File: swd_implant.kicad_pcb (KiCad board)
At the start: 2 copper layers, 13.9 x 38.5 mm, 28 parts, among them J1 U262-161N-4BVC11, J2 G&W pressure contact, J3 50 mil Pin Header, J4 SOICbite, J5 100 mil Pin Header, J6 100 mil Pin header, U1 ATSAMD21E18A, U2 AP2127K-3.3

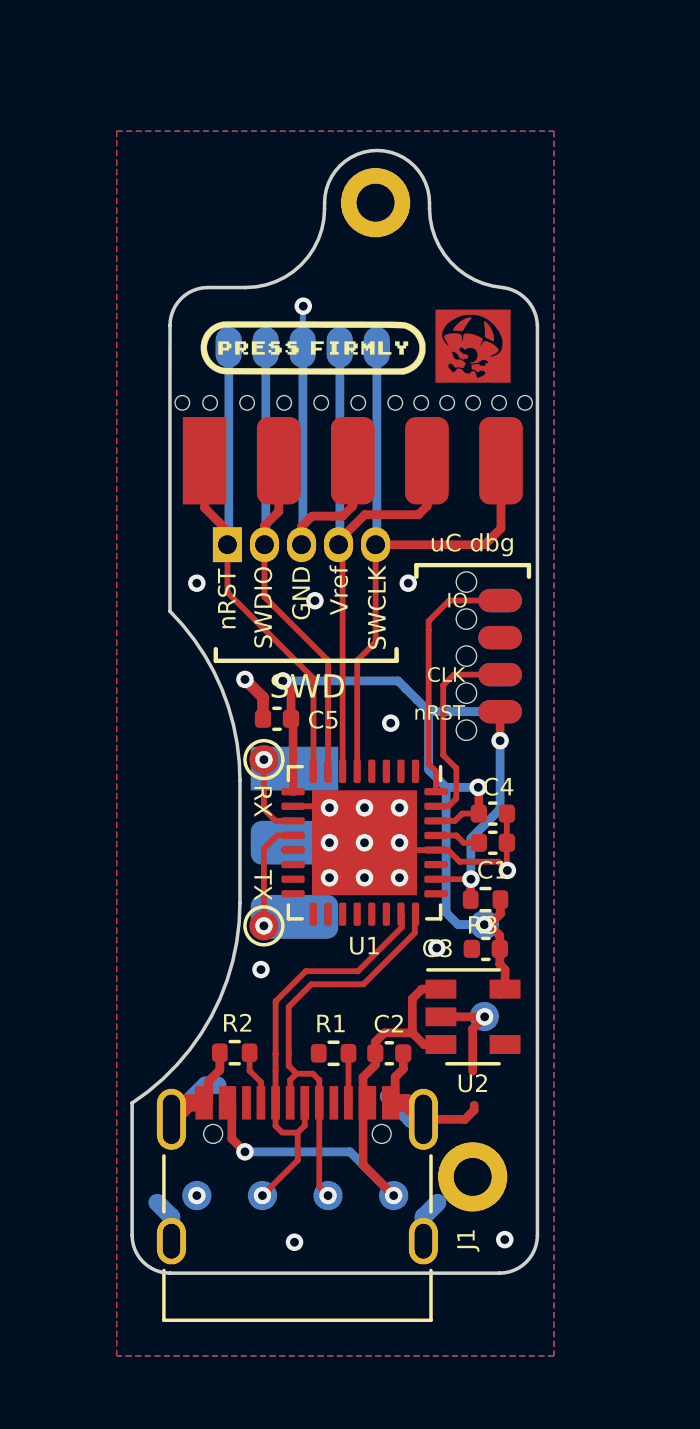
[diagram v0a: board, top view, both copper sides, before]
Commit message: New board outline & swd pinout fixes
Changed the board outline to work with castellated edges, making it possible to
solder down instead of just relying on pressure contact.

Also fixed the inverted SWD pinout from upstream.
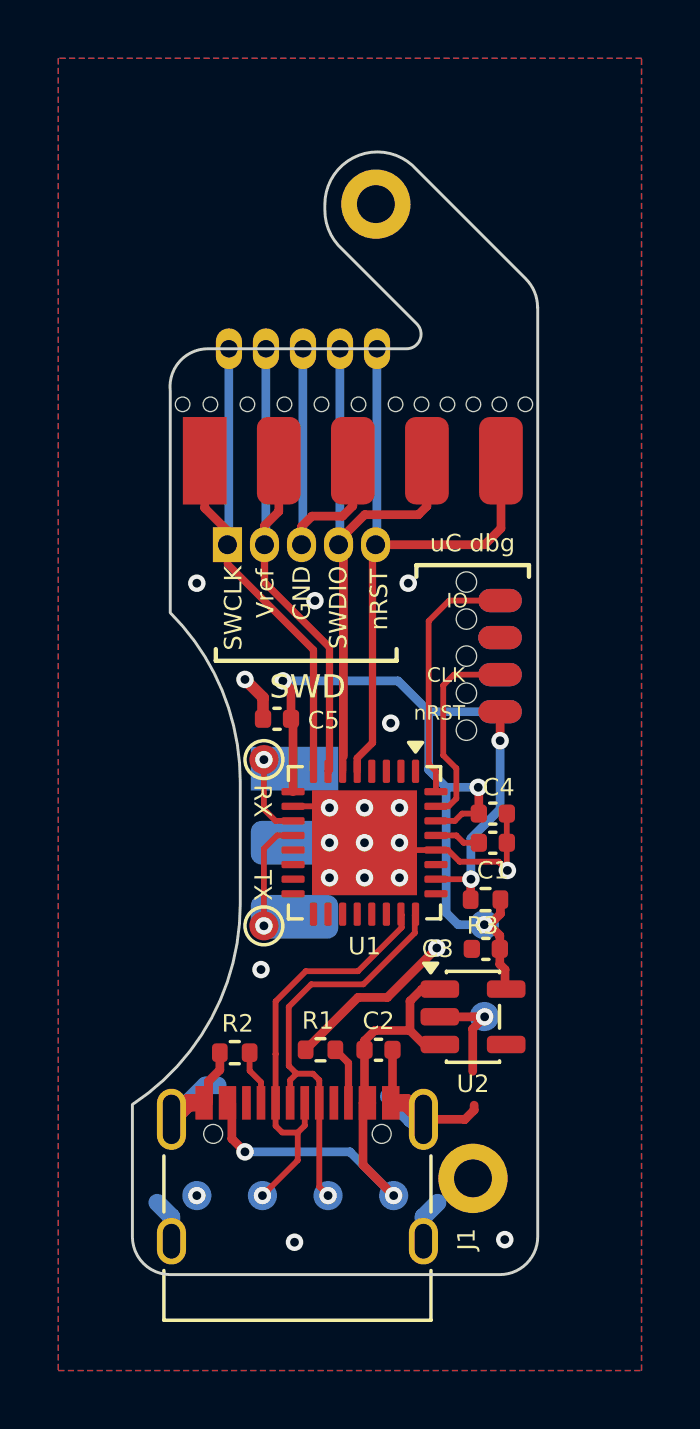
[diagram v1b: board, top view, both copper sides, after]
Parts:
- removed the Ref** at (64.2, 99.9)
- removed the Ref** at (58.7, 99.9)
- removed the Ref** at (59.2, 123.0)
- J2: value G&W pressure contact -> G&W pressure contact
- moved R1 0.47 mm to (59.0, 124.0)
- moved Ref** 0.43 mm to (60.2, 104.7)
- moved C2 0.39 mm to (61.0, 124.0)
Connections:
- net /~RESET~ renamed /~{RESET}
- J1 pad A8: no_connect_18 -> unconnected-(J1-SBU1-PadA8)
- J1 pad B8: no_connect_19 -> unconnected-(J1-SBU2-PadB8)
- J2 pad 1: /GnW_NRST -> /GnW_SWCLK
- J2 pad 2: /GnW_SWDIO -> /GnW_Vref
- J2 pad 4: /GnW_Vref -> /GnW_SWDIO
- J2 pad 5: /GnW_SWCLK -> /GnW_NRST
- J2 pad 6: GND -> (no net)
- J3 pad 1: /GnW_NRST -> /GnW_SWCLK
- J3 pad 2: /GnW_SWDIO -> /GnW_Vref
- J3 pad 4: /GnW_Vref -> /GnW_SWDIO
- J3 pad 5: /GnW_SWCLK -> /GnW_NRST
- J4 pad 2: no_connect_20 -> unconnected-(J4-Pin_2-Pad2)
- J4 pad 3: no_connect_21 -> unconnected-(J4-Pin_3-Pad3)
- J4 pad 6: no_connect_22 -> unconnected-(J4-Pin_6-Pad6)
- J5 pad 1: /GnW_NRST -> /GnW_SWCLK
- J5 pad 2: /GnW_SWDIO -> /GnW_Vref
- J5 pad 4: /GnW_Vref -> /GnW_SWDIO
- J5 pad 5: /GnW_SWCLK -> /GnW_NRST
- U1 pad 1: no_connect_23 -> unconnected-(U1-PA00-Pad1)
- U1 pad 13: no_connect_24 -> unconnected-(U1-PA10-Pad13)
- U1 pad 14: no_connect_25 -> unconnected-(U1-PA11-Pad14)
- U1 pad 15: no_connect_26 -> unconnected-(U1-PA14-Pad15)
- U1 pad 16: no_connect_27 -> unconnected-(U1-PA15-Pad16)
- U1 pad 17: no_connect_28 -> unconnected-(U1-PA16-Pad17)
- U1 pad 18: no_connect_29 -> unconnected-(U1-PA17-Pad18)
- U1 pad 19: no_connect_30 -> unconnected-(U1-PA18-Pad19)
- U1 pad 2: no_connect_31 -> unconnected-(U1-PA01-Pad2)
- U1 pad 20: no_connect_32 -> unconnected-(U1-PA19-Pad20)
- U1 pad 21: no_connect_33 -> unconnected-(U1-PA22-Pad21)
- U1 pad 22: no_connect_34 -> unconnected-(U1-PA23-Pad22)
- U1 pad 25: no_connect_35 -> unconnected-(U1-PA27-Pad25)
- U1 pad 27: no_connect_36 -> unconnected-(U1-PA28-Pad27)
- U1 pad 3: no_connect_37 -> unconnected-(U1-PA02-Pad3)
- U1 pad 4: no_connect_38 -> unconnected-(U1-PA03-Pad4)
- U1 pad 5: /GnW_SWCLK -> /GnW_NRST
- U1 pad 6: /GnW_Vref -> /GnW_SWDIO
- U1 pad 7: /GnW_SWDIO -> /GnW_Vref
- U1 pad 8: /GnW_NRST -> /GnW_SWCLK
- U2 pad 4: (no net) -> unconnected-(U2-NC-Pad4)
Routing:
- net GND: track 48.5 -> 51.6 mm, vias 22 -> 21
- net /GnW_NRST: track 19.0 -> 21.8 mm
- net /GnW_SWCLK: track 21.8 -> 19.0 mm
- net /GnW_SWDIO: track 18.5 -> 20.2 mm
- net /GnW_Vref: track 20.1 -> 18.6 mm
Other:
- outline, holes or cut-outs redrawn
- board text added: "G&W ${VERSION}"

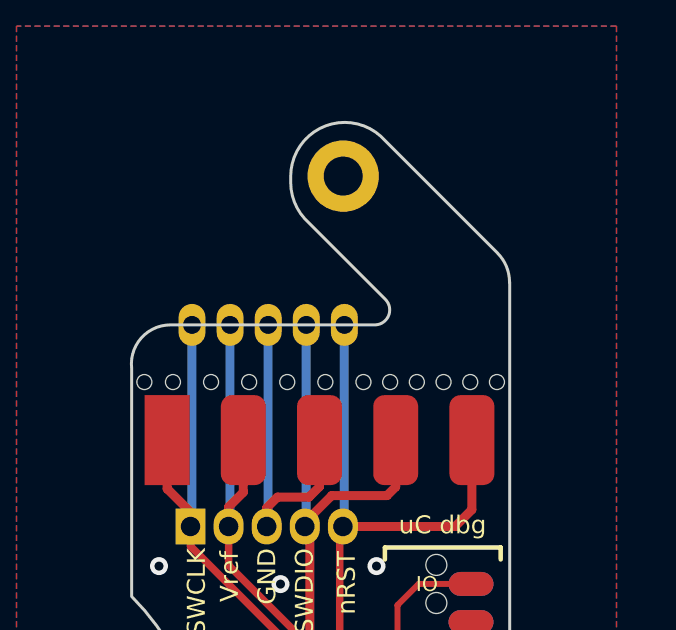
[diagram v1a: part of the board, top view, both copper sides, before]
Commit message: Add M marker to front of board
This M is to indicate that it is the "Mario" variant of the implant
board.
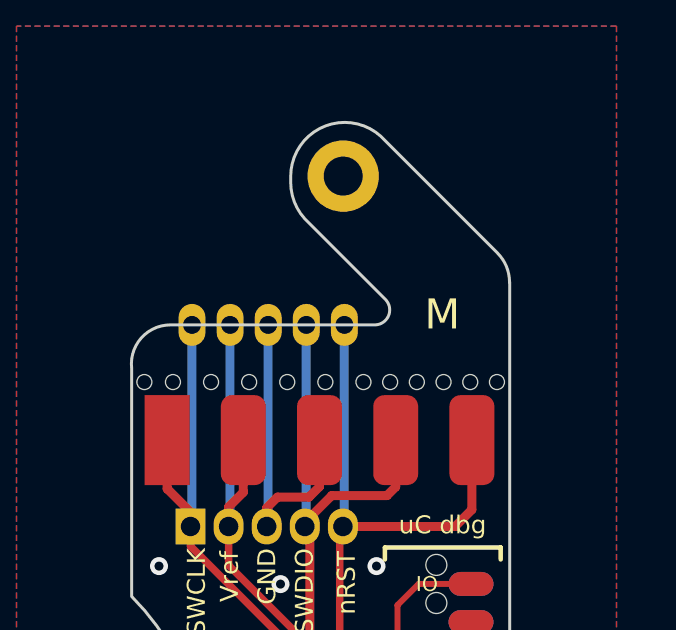
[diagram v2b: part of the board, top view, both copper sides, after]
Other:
- board text added: "M"
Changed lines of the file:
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@@
+		)
+	)
+	(gr_text "M"
+		(at 63.6 100.2 0)
+		(layer "F.SilkS")
+		(effects
+			(font
+				(size 1 1)
+				(thickness 0.15)
+			)
+			(justify left bottom)
 		)
 	)

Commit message: Prep for fabrication
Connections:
- J2 pad 6: (no net) -> GND
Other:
- board text added: "${TITLE} ${VERSION}"
- board text added: "JLCJLCJLC"
- board text added: "REV:${REV}"
- board text removed: "G&W ${VERSION}"
- board text removed: "M"
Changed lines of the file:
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@@
 		)
 	)
+	(property "REV" "m1")
+	(property "TITLE" "G&W SWD")
 	(property "VERSION" "Mario")
 	(net 0 "")
@@
 		(sheetname "/")
 		(sheetfile "swd_implant.kicad_sch")
-		(attr exclude_from_pos_files)
+		(attr exclude_from_pos_files exclude_from_bom)
 		(fp_circle
 			(center 0 0)
@@
 		(sheetname "/")
 		(sheetfile "swd_implant.kicad_sch")
-		(attr through_hole)
+		(attr through_hole exclude_from_pos_files exclude_from_bom dnp)
 		(fp_poly
 			(pts
@@
 			(layers "*.Cu" "*.Mask")
 			(remove_unused_layers no)
+			(net 1 "GND")
 			(clearance 0)
 			(zone_connect 2)
@@
 		(sheetname "/")
 		(sheetfile "swd_implant.kicad_sch")
-		(attr exclude_from_pos_files)
+		(attr exclude_from_pos_files exclude_from_bom)
 		(fp_circle
 			(center 0 0)
@@
 		(sheetname "/")
 		(sheetfile "swd_implant.kicad_sch")
-		(attr through_hole)
+		(attr through_hole exclude_from_pos_files exclude_from_bom dnp)
 		(fp_line
 			(start 1.55 -1.15)
@@
 		(sheetname "/")
 		(sheetfile "swd_implant.kicad_sch")
-		(attr through_hole)
+		(attr through_hole exclude_from_pos_files exclude_from_bom dnp)
 		(fp_line
 			(start 1.27 0.381)
@@
 		(sheetname "/")
 		(sheetfile "swd_implant.kicad_sch")
-		(attr exclude_from_pos_files)
+		(attr exclude_from_pos_files exclude_from_bom)
 		(fp_circle
 			(center 0 0)
@@
 		(sheetname "/")
 		(sheetfile "swd_implant.kicad_sch")
-		(attr exclude_from_pos_files)
+		(attr exclude_from_pos_files exclude_from_bom)
 		(fp_circle
 			(center 0 0)
@@
 		(sheetname "/")
 		(sheetfile "swd_implant.kicad_sch")
-		(attr exclude_from_pos_files)
+		(attr exclude_from_pos_files exclude_from_bom)
 		(fp_circle
 			(center 0 0)
@@
 		)
 	)
-	(gr_text "M"
-		(at 63.6 100.2 0)
+	(gr_text "REV:${REV}"
+		(at 61.3 97 315)
 		(layer "F.SilkS")
 		(effects
@@
 		)
 	)
+	(gr_text "JLCJLCJLC"
+		(at 65.7 125 0)
+		(layer "B.SilkS")
+		(effects
+			(font
+				(size 1 1)
+				(thickness 0.15)
+			)
+			(justify left bottom mirror)
+		)
+	)
 	(gr_text "UART"
 		(at 62.8 116.9 270)
@@
 		)
 	)
-	(gr_text "G&W ${VERSION}"
-		(at 66 103.8 0)
+	(gr_text "${TITLE} ${VERSION}"
+		(at 66.2 103.8 0)
 		(layer "B.SilkS")
 		(effects

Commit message: more fabrication updates
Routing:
- net /TX: track 3.84 -> 5.01 mm
- net /RX: track 2.87 -> 4.04 mm

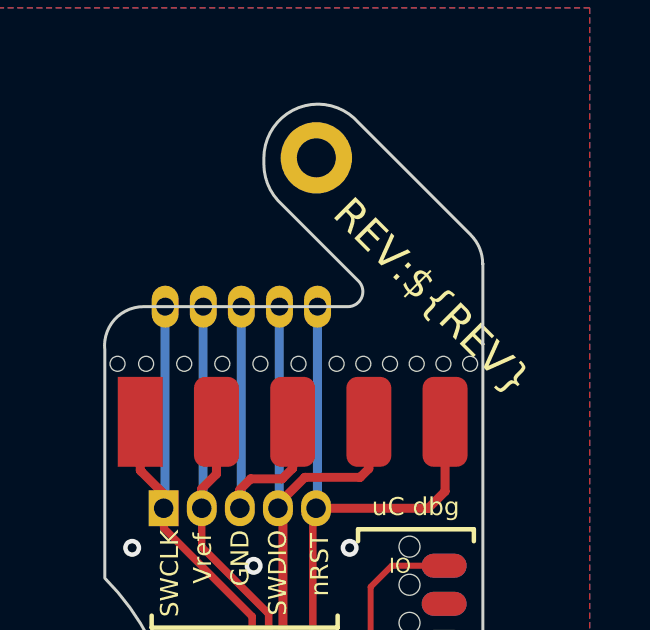
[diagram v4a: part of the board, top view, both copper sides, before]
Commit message: Add logos
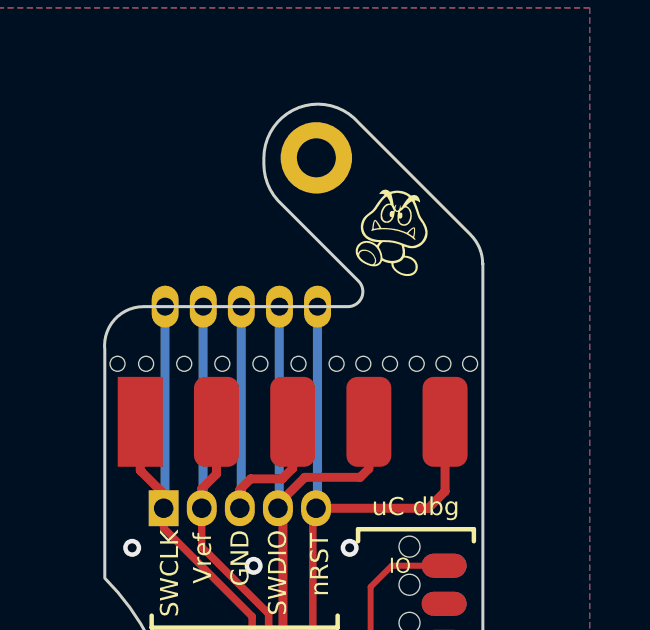
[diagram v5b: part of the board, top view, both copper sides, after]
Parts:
- added G***: LOGO, LOGO, F.Cu at (62.9, 97.6)
- added Q**: Qwindelzorf, qwindelzorf:qwindelzorf_1520, B.Cu at (70.3, 87.0)
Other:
- board text added: "JLCJLCJLCJLC"
- board text removed: "JLCJLCJLC"
